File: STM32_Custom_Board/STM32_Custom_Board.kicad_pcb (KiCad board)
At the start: 2 copper layers, 0 parts

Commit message: Decoupling capacitors positioned in PCB
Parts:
- added C1: 22u, Capacitor_SMD:C_0805_2012Metric, F.Cu at (163.3, 64.2)
- added C10: 1u, Capacitor_SMD:C_0402_1005Metric, F.Cu at (157.0, 86.3)
- added C11: 100n, Capacitor_SMD:C_0402_1005Metric, F.Cu at (157.0, 88.2)
- added C12: 10p, Capacitor_SMD:C_0402_1005Metric, F.Cu at (157.0, 90.2)
- added C13: 10p, Capacitor_SMD:C_0402_1005Metric, F.Cu at (157.0, 92.2)
- added C2: 22u, Capacitor_SMD:C_0805_2012Metric, F.Cu at (163.3, 67.2)
- added C3: 10u, Capacitor_SMD:C_0603_1608Metric, F.Cu at (163.1, 70.0)
- added C4: 100n, Capacitor_SMD:C_0402_1005Metric, F.Cu at (83.5, 73.5)
- added C5: 100n, Capacitor_SMD:C_0402_1005Metric, F.Cu at (94.5, 83.0)
- added C6: 100n, Capacitor_SMD:C_0402_1005Metric, F.Cu at (98.5, 74.0)
- added C7: 100n, Capacitor_SMD:C_0402_1005Metric, F.Cu at (89.5, 70.5)
- added C8: 10n, Capacitor_SMD:C_0402_1005Metric, F.Cu at (154.1, 92.2)
- added C9: 1u, Capacitor_SMD:C_0402_1005Metric, F.Cu at (157.0, 84.3)
- added D1: RED, LED_SMD:LED_0603_1608Metric, F.Cu at (162.8, 81.0)
- added FB1: 120R, Inductor_SMD:L_0603_1608Metric, F.Cu at (163.1, 72.5)
- added J1: USB_B_Micro, Connector_USB:USB_Micro-B_Wuerth_629105150521, F.Cu at (155.2, 77.9)
- added J2: Conn_01x04_Male, Connector_PinHeader_2.54mm:PinHeader_1x04_P2.54mm_Vertical, F.Cu at (136.4, 82.9)
- added J3: Conn_01x04_Male, Connector_PinHeader_2.54mm:PinHeader_1x04_P2.54mm_Vertical, F.Cu at (141.0, 82.9)
- added J4: Conn_01x04_Male, Connector_PinHeader_2.54mm:PinHeader_1x04_P2.54mm_Vertical, F.Cu at (145.6, 82.9)
- added R1: 1k5, Resistor_SMD:R_0402_1005Metric, F.Cu at (151.2, 84.3)
- added R2: 10k, Resistor_SMD:R_0402_1005Metric, F.Cu at (151.2, 86.3)
- added R3: 1k5, Resistor_SMD:R_0402_1005Metric, F.Cu at (151.2, 88.3)
- added R4: 1k5, Resistor_SMD:R_0402_1005Metric, F.Cu at (151.2, 90.3)
- added R5: 1k5, Resistor_SMD:R_0402_1005Metric, F.Cu at (151.2, 92.3)
- added SW1: SW_SPDT, Button_Switch_THT:SW_E-Switch_EG1224_SPDT_Angled, F.Cu at (138.0, 66.3)
- added U1: AMS1117-3.3, Package_TO_SOT_SMD:SOT-223-3_TabPin2, F.Cu at (163.3, 87.5)
- added U2: STM32F103C8T6, Package_QFP:LQFP-48_7x7mm_P0.5mm, F.Cu at (91.7, 76.8)
- added Y1: 16MHz, Crystal:Crystal_SMD_3225-4Pin_3.2x2.5mm_HandSoldering, F.Cu at (164.0, 76.9)

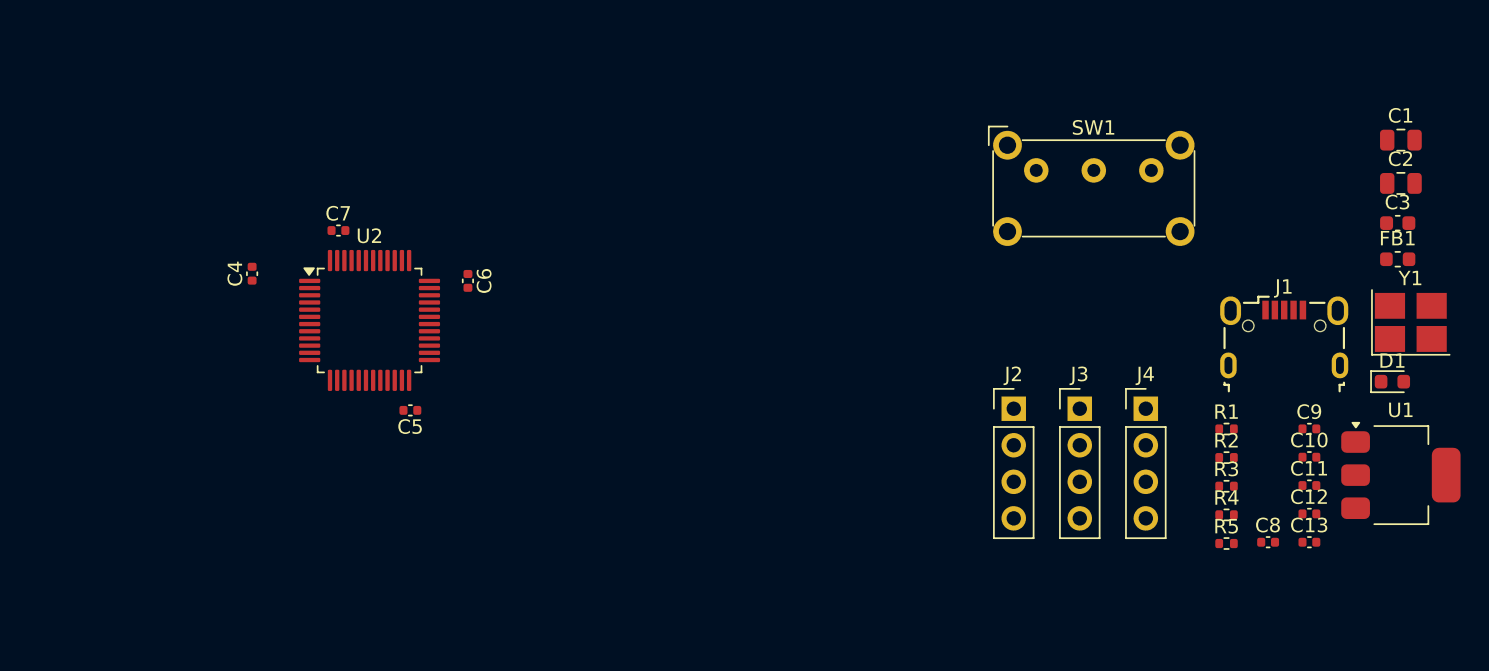
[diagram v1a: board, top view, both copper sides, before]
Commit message: Component placement finished
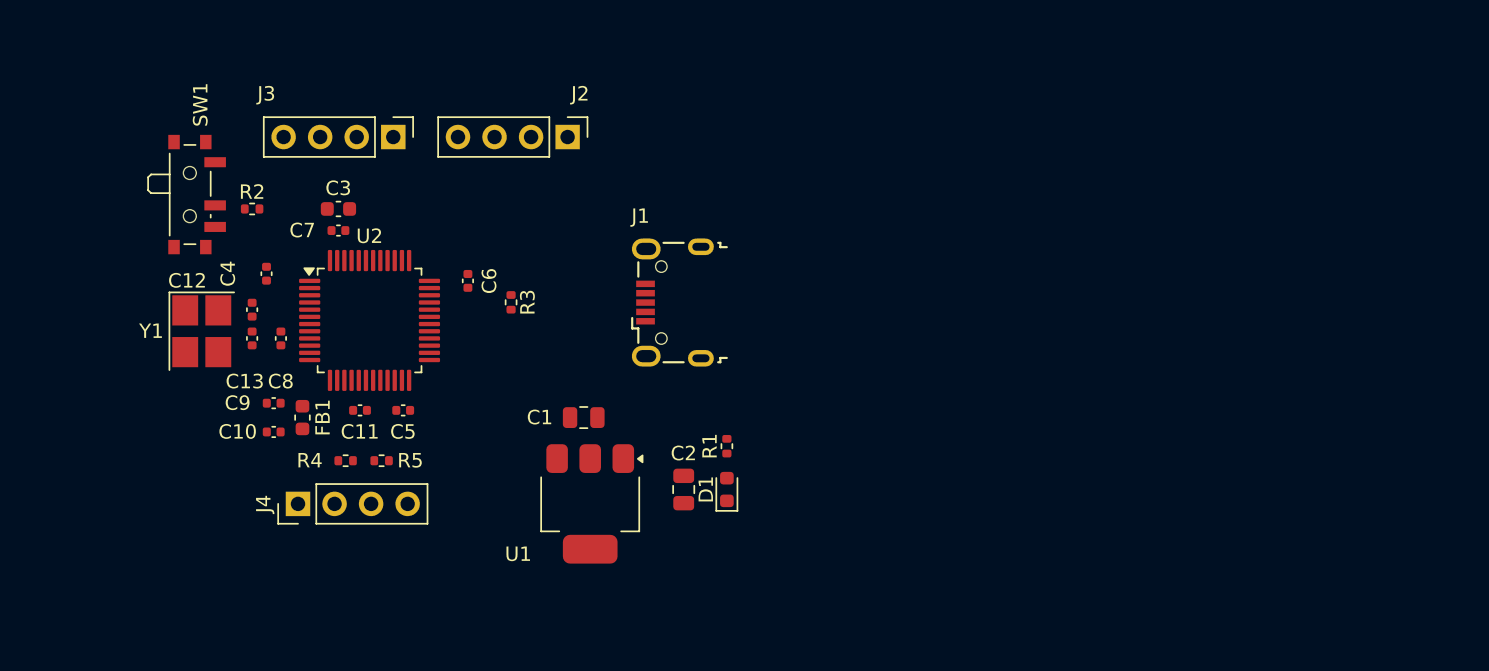
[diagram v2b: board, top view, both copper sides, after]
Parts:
- SW1: footprint Button_Switch_THT:SW_E-Switch_EG1224_SPDT_Angled -> Button_Switch_SMD:SW_SPDT_PCM12
- moved Y1 84.0 mm to (80.0, 77.5), turned to -90 degrees
- moved FB1 76.9 mm to (87.0, 83.5), turned to -90 degrees
- moved C12 74.8 mm to (83.5, 76.0), turned to 90 degrees
- moved C13 74.8 mm to (83.5, 78.0), turned to 90 degrees
- moved C3 73.6 mm to (89.5, 69.0)
- moved C9 72.0 mm to (85.0, 82.5), turned to 180 degrees
- moved C10 72.0 mm to (85.0, 84.5), turned to 180 degrees
- moved C8 70.1 mm to (85.5, 78.0), turned to 90 degrees
- moved R2 69.9 mm to (83.5, 69.0)
- moved C11 66.2 mm to (91.0, 83.0)
- moved R4 61.3 mm to (90.0, 86.5), turned to 180 degrees
- moved C1 60.0 mm to (106.5, 83.5)
- moved J4 59.3 mm to (86.7, 89.5), turned to 90 degrees
- moved R5 59.0 mm to (92.5, 86.5), turned to 180 degrees
- moved SW1 58.5 mm to (79.5, 68.0), turned to -90 degrees
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
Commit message: Board outline finished and connectors put in place
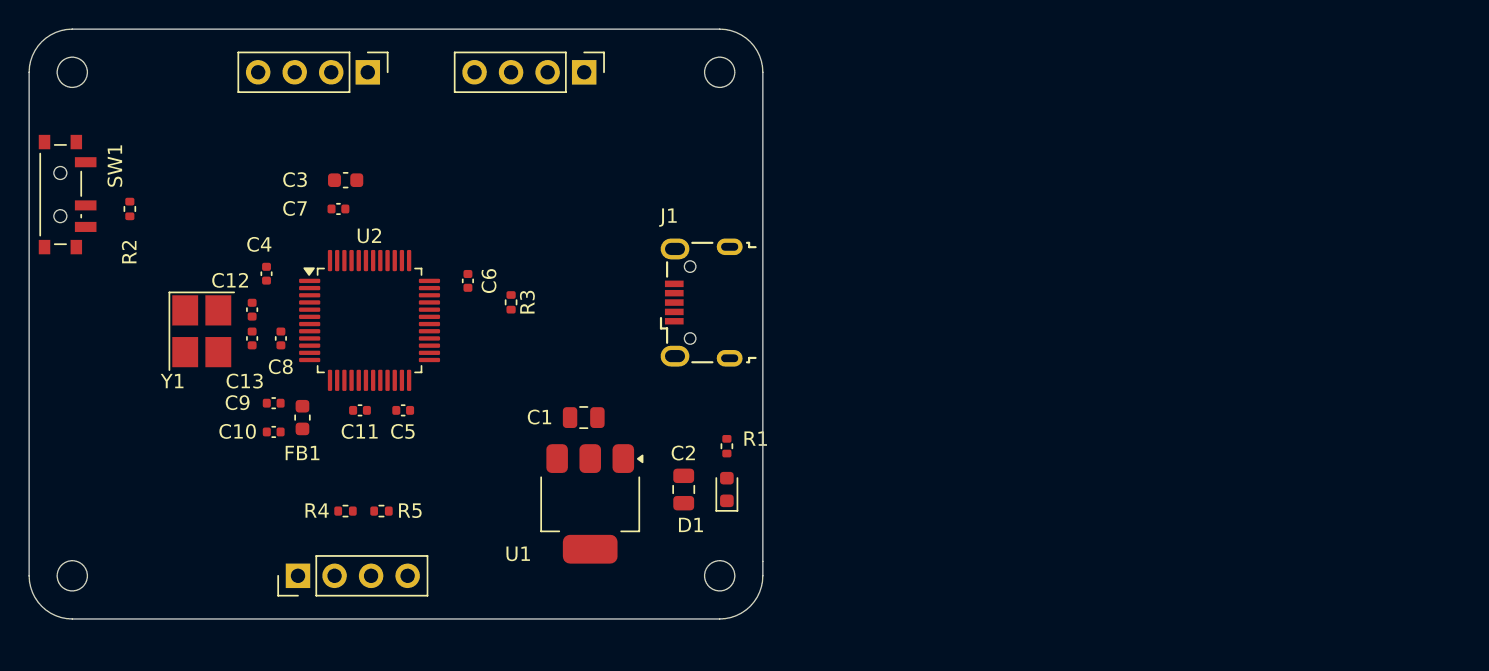
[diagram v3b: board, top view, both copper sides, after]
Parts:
- added H1: MountingHole, MountingHole:MountingHole_2.1mm, F.Cu at (71.0, 94.5)
- added H2: MountingHole, MountingHole:MountingHole_2.1mm, F.Cu at (116.0, 94.5)
- added H3: MountingHole, MountingHole:MountingHole_2.1mm, F.Cu at (71.0, 59.5)
- added H4: MountingHole, MountingHole:MountingHole_2.1mm, F.Cu at (116.0, 59.5)
- moved SW1 9.00 mm to (70.5, 68.0)
- moved R2 8.50 mm to (75.0, 69.0), turned to 90 degrees
- moved J4 5.00 mm to (86.7, 94.5)
- moved J3 4.84 mm to (91.5, 59.5)
- moved J2 4.64 mm to (106.6, 59.5)
- moved R4 3.50 mm to (90.0, 90.0)
- moved R5 3.50 mm to (92.5, 90.0)
- moved C3 2.06 mm to (90.0, 67.0)
- moved J1 2.00 mm to (114.7, 75.5)
- moved C7 1.50 mm to (89.5, 69.0)
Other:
- board outline added: 51 x 41 mm

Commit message: Routing of signals finished
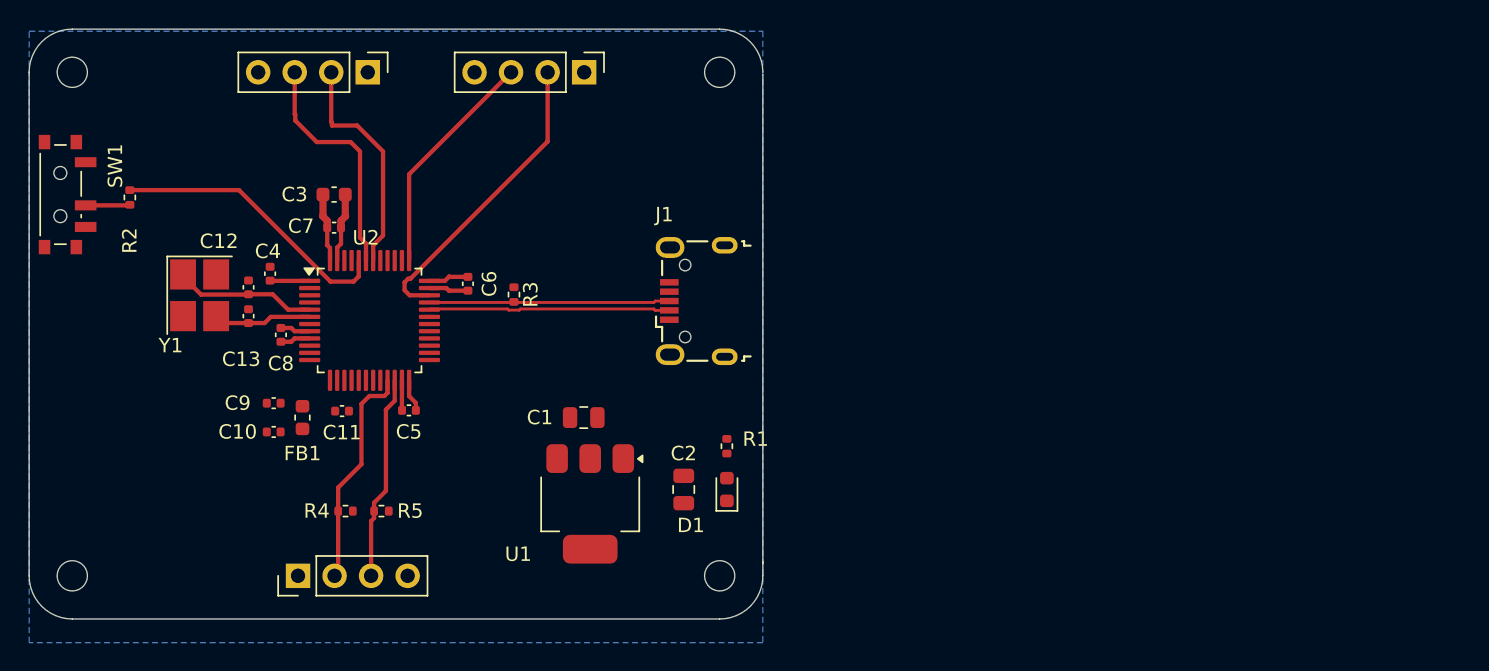
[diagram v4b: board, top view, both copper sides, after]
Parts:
- moved Y1 2.50 mm to (79.8, 75.0)
- moved C12 1.57 mm to (83.2, 74.5)
- moved C13 1.57 mm to (83.2, 76.5)
- moved C7 1.33 mm to (89.2, 70.3)
- moved C3 1.28 mm to (89.2, 68.0)
- moved C11 1.25 mm to (89.8, 83.0)
- moved R2 0.80 mm to (75.0, 68.2)
- moved R3 0.58 mm to (101.7, 75.0)
- moved C5 0.40 mm to (94.4, 83.0)
- moved J1 0.36 mm to (114.4, 75.4)
- moved C4 0.25 mm to (84.8, 73.5)
- moved C8 0.25 mm to (85.5, 77.8)
- moved C6 0.20 mm to (98.5, 74.2)
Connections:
- U2 pad 31: /USB_D- -> unconnected-(U2-PA10-Pad31)
- U2 pad 32: /USB_D+ -> /USB_D-
- U2 pad 33: /SWDIO -> /USB_D+
- U2 pad 34: /SWCLK -> /SWDIO
- U2 pad 37: unconnected-(U2-PA14-Pad37) -> /SWCLK
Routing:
- net /SWDIO: track 0.00 -> 21.2 mm
- net /BOOT0: track 0.00 -> 19.8 mm
- net /USB_D-: track 0.00 -> 16.8 mm
- net /USB_D+: track 0.00 -> 16.7 mm
- net /USART_RX: track 0.00 -> 16.5 mm
- net /SWCLK: track 0.00 -> 16.0 mm
- net /USART1_TX: track 0.00 -> 15.9 mm
- net /I2CS_SCL: track 0.00 -> 15.7 mm
- net /I2CS_SDA: track 0.00 -> 14.3 mm
- net +3.3V: track 0.00 -> 12.7 mm
- net GND: track 0.00 -> 11.8 mm
- net /HSE_IN: track 0.00 -> 9.92 mm
- net /HSE_OUT: track 0.00 -> 6.88 mm
- net /SW_BOOT0: track 0.00 -> 3.09 mm
- net +3.3VA: track 0.00 -> 2.10 mm
- added copper zone on B.Cu, net GND
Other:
- outline, holes or cut-outs redrawn

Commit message: Routing process finished
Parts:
- moved D1 2.24 mm to (114.5, 87.5), turned to -90 degrees
- moved C2 1.80 mm to (112.0, 87.5)
- moved R1 1.80 mm to (115.0, 84.5), turned to 0 degrees
- moved R4 0.70 mm to (89.3, 89.9), turned to 0 degrees
- moved C11 0.35 mm to (89.4, 83.0)
- moved C10 0.20 mm to (85.0, 84.3)
- moved C9 0.20 mm to (85.0, 82.7)
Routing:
- net +3.3V: track 12.7 -> 189.5 mm
- net GND: track 11.8 -> 38.3 mm, vias 0 -> 19
- net /NRST: track 0.00 -> 12.5 mm
- net +3.3VA: track 2.10 -> 8.22 mm
- net /BOOT0: vias 0 -> 2
- added copper zone on F.Cu, net +3.3V
- added copper zone on F.Cu, net GND
- added copper zone on F.Cu, net VBUS

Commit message: PCB board finished
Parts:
- moved R3 1.30 mm to (103.0, 75.0)
- moved C8 0.90 mm to (85.0, 78.5)
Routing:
- net /PWR_LED_K: track 0.00 -> 2.22 mm
- net +3.3V: track 189.5 -> 190.8 mm
- net GND: track 38.3 -> 39.5 mm, vias 19 -> 20
- net /BOOT0: track 19.8 -> 20.9 mm
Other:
- outline, holes or cut-outs redrawn
- board text added: "1"
- board text added: "SWD"
- board text added: "UART"
- board text added: "V1 06/2025"

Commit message: Image added to the PCB
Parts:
- added G***: LOGO, LOGO, F.Cu at (71.0, 88.0)
